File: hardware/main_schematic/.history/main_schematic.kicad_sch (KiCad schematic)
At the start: 0 parts

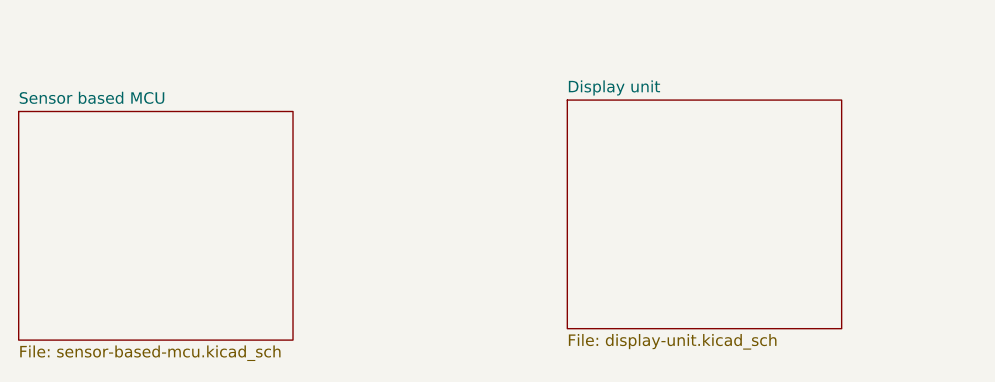
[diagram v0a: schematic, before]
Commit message: Schematic done
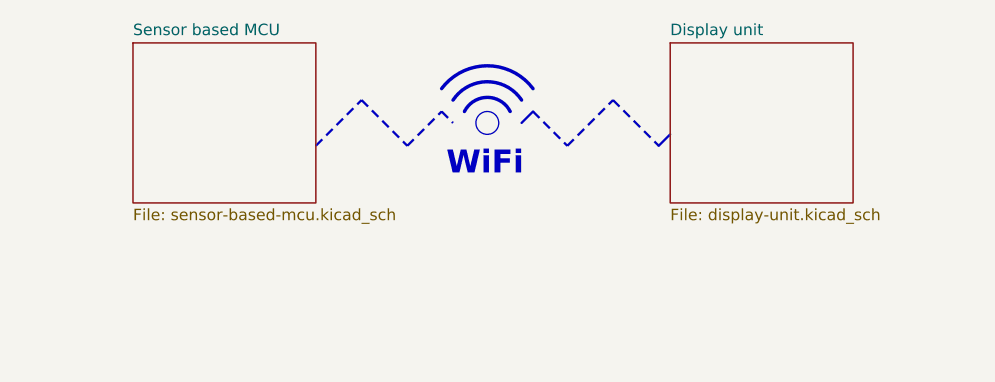
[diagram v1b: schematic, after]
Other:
- note added: "WiFi"
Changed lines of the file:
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@@
 		(company "Marcel Siwiela")
 	)
+	(circle
+		(center 101.6 63.5)
+		(radius 1.27)
+		(stroke
+			(width 0)
+			(type solid)
+			(color 0 0 255 1)
+		)
+		(fill
+			(type color)
+			(color 0 0 0 0)
+		)
+	)
+	(arc
+		(start 96.5201 59.6899)
+		(mid 101.6001 57.15)
+		(end 106.68 59.69)
+		(stroke
+			(width 0.381)
+			(type solid)
+		)
+		(fill
+			(type none)
+		)
+	)
+	(arc
+		(start 97.79 60.96)
+		(mid 101.6 58.9209)
+		(end 105.4101 60.96)
+		(stroke
+			(width 0.381)
+			(type solid)
+		)
+		(fill
+			(type none)
+		)
+	)
+	(arc
+		(start 99.06 62.23)
+		(mid 101.6 60.6602)
+		(end 104.14 62.23)
+		(stroke
+			(width 0.381)
+			(type solid)
+		)
+		(fill
+			(type none)
+		)
+	)
+	(text "WiFi\n"
+		(exclude_from_sim no)
+		(at 101.346 68.072 0)
+		(effects
+			(font
+				(size 2.54 2.54)
+				(thickness 0.508)
+				(bold yes)
+			)
+		)
+	)
+	(polyline
+		(pts
+			(xy 96.52 62.23) (xy 97.79 63.5)
+		)
+		(stroke
+			(width 0.254)
+			(type dash)
+		)
+	)
+	(polyline
+		(pts
+			(xy 120.65 66.04) (xy 121.92 64.77)
+		)
+		(stroke
+			(width 0.254)
+			(type solid)
+		)
+	)
+	(polyline
+		(pts
+			(xy 105.41 63.5) (xy 106.68 62.23)
+		)
+		(stroke
+			(width 0.254)
+			(type solid)
+		)
+	)
+	(polyline
+		(pts
+			(xy 87.63 60.96) (xy 92.71 66.04)
+		)
+		(stroke
+			(width 0.254)
+			(type dash)
+		)
+	)
+	(polyline
+		(pts
+			(xy 92.71 66.04) (xy 96.52 62.23)
+		)
+		(stroke
+			(width 0.254)
+			(type dash)
+		)
+	)
+	(polyline
+		(pts
+			(xy 115.57 60.96) (xy 120.65 66.04)
+		)
+		(stroke
+			(width 0.254)
+			(type dash)
+		)
+	)
+	(polyline
+		(pts
+			(xy 110.49 66.04) (xy 115.57 60.96)
+		)
+		(stroke
+			(width 0.254)
+			(type dash)
+		)
+	)
+	(polyline
+		(pts
+			(xy 106.68 62.23) (xy 110.49 66.04)
+		)
+		(stroke
+			(width 0.254)
+			(type dash)
+		)
+	)
+	(polyline
+		(pts
+			(xy 82.55 66.04) (xy 87.63 60.96)
+		)
+		(stroke
+			(width 0.254)
+			(type dash)
+		)
+	)
 	(sheet
-		(at 110.49 60.96)
-		(size 30.48 25.4)
+		(at 121.92 54.61)
+		(size 20.32 17.78)
 		(exclude_from_sim no)
 		(in_bom yes)
@@
 		)
 		(property "Sheetname" "Display unit"
-			(at 110.49 60.2484 0)
+			(at 121.92 53.8984 0)
 			(show_name no)
 			(do_not_autoplace no)
@@
 		)
 		(property "Sheetfile" "display-unit.kicad_sch"
-			(at 110.49 86.9446 0)
+			(at 121.92 72.9746 0)
 			(show_name no)
 			(do_not_autoplace no)
@@
 	)
 	(sheet
-		(at 49.53 62.23)
-		(size 30.48 25.4)
+		(at 62.23 54.61)
+		(size 20.32 17.78)
 		(exclude_from_sim no)
 		(in_bom yes)
@@
 		)
 		(property "Sheetname" "Sensor based MCU"
-			(at 49.53 61.5184 0)
+			(at 62.23 53.8984 0)
 			(show_name no)
 			(do_not_autoplace no)
@@
 		)
 		(property "Sheetfile" "sensor-based-mcu.kicad_sch"
-			(at 49.53 88.2146 0)
-			(show_name no)
-			(do_not_autoplace no)
+			(at 62.23 72.9746 0)
+			(show_name no)
+			(do_not_autoplace no)
